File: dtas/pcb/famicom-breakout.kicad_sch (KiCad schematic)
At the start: 20 parts

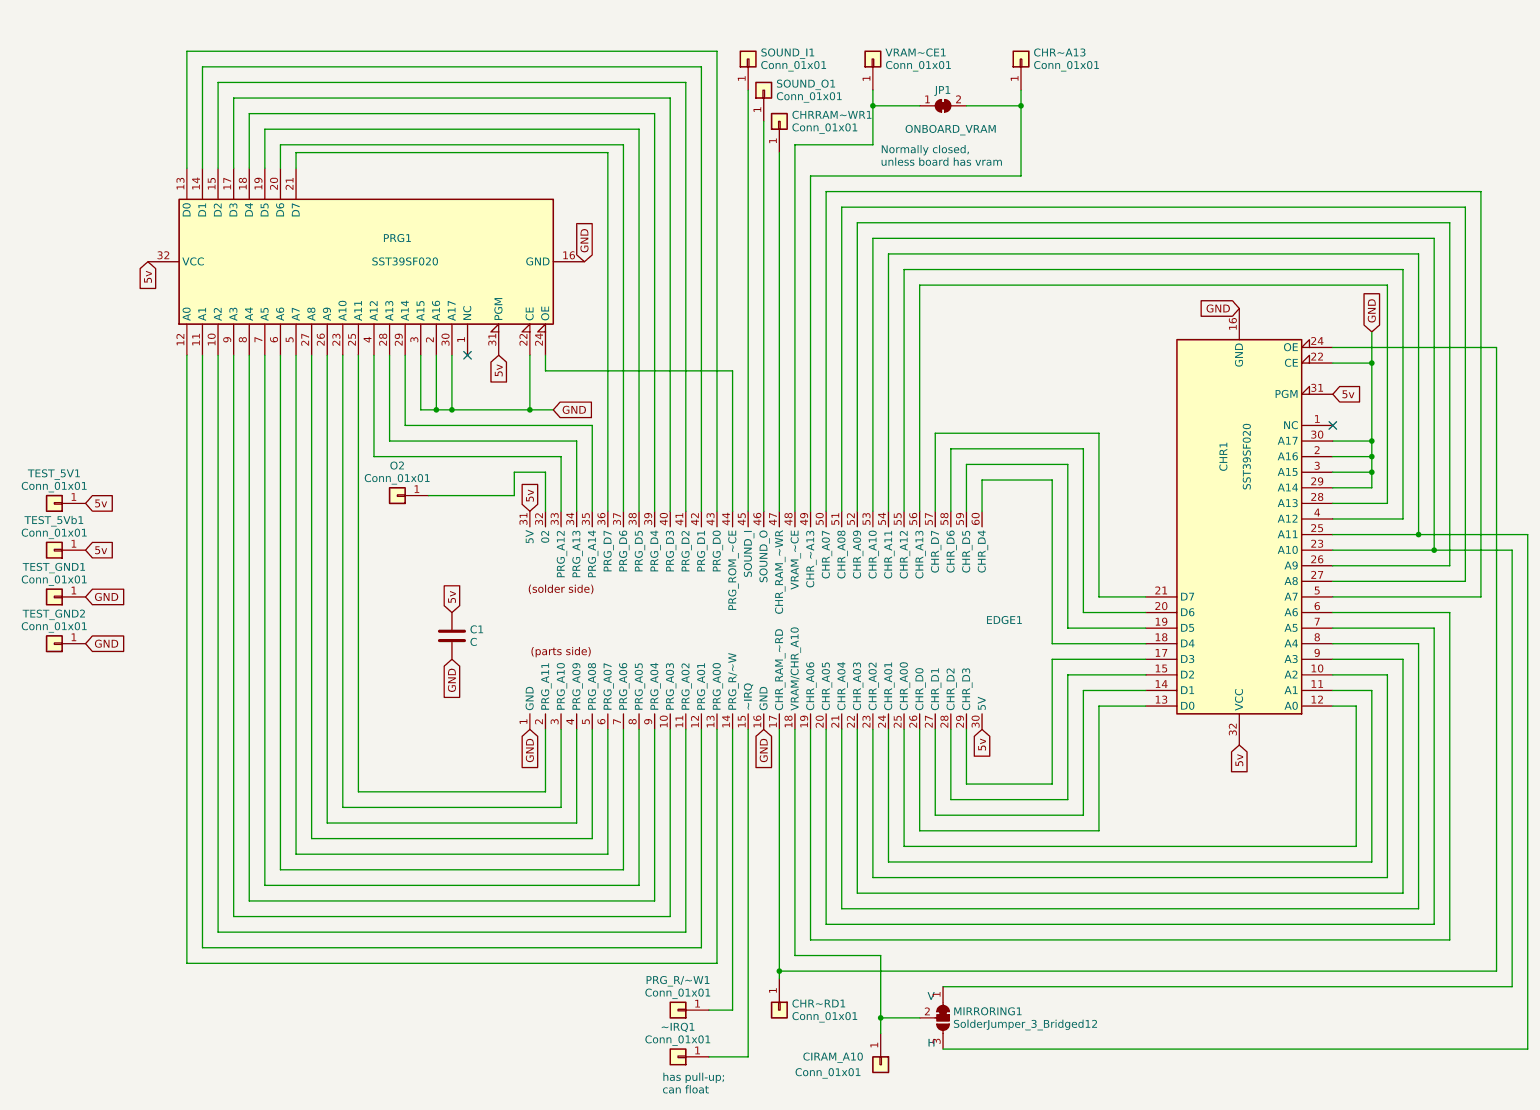
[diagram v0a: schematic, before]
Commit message: Version 2 of board, which just adds many additional test points and jumpers so I can debug the thing
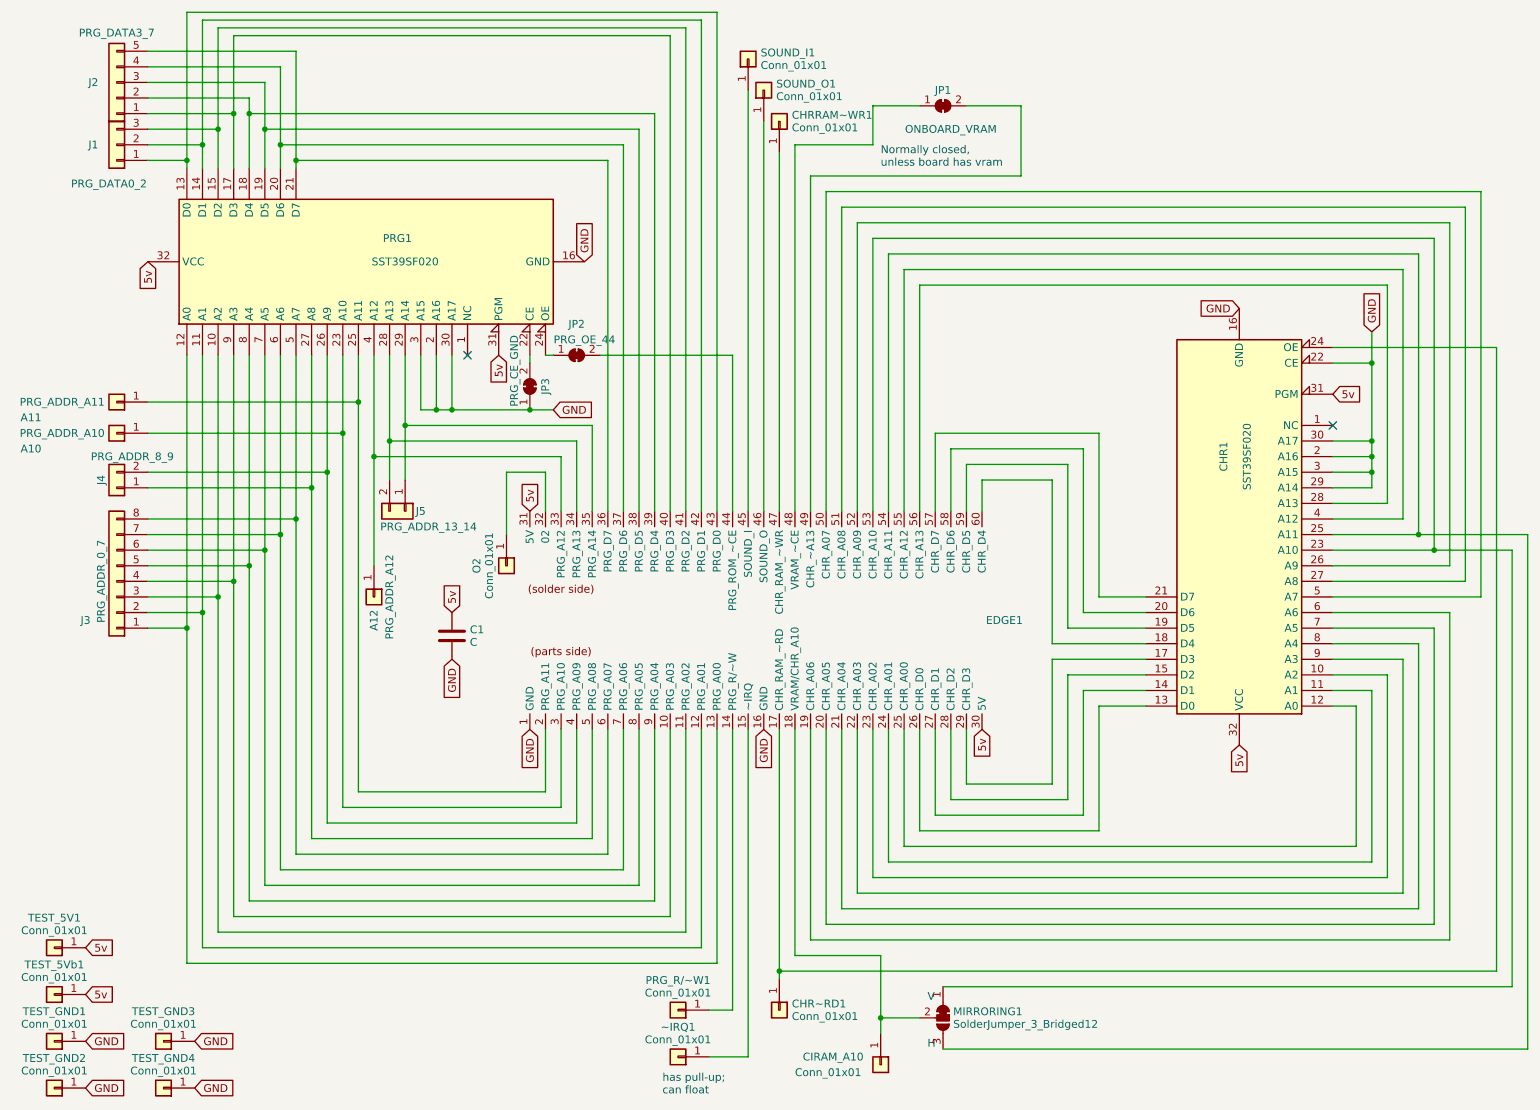
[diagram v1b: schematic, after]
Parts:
- removed CHR~A13, VRAM~CE1: Conn_01x01, Connector_PinHeader_2.54mm:PinHeader_1x01_P2.54mm_Vertical, symbol Connector_Generic:Conn_01x01
- added A10: PRG_ADDR_A10, Connector_PinHeader_2.54mm:PinHeader_1x01_P2.54mm_Vertical, symbol Connector_Generic:Conn_01x01
- added A11: PRG_ADDR_A11, Connector_PinHeader_2.54mm:PinHeader_1x01_P2.54mm_Vertical, symbol Connector_Generic:Conn_01x01
- added A12: PRG_ADDR_A12, Connector_PinHeader_2.54mm:PinHeader_1x01_P2.54mm_Vertical, symbol Connector_Generic:Conn_01x01
- added J1: PRG_DATA0_2, Connector_PinHeader_2.54mm:PinHeader_1x03_P2.54mm_Vertical, symbol Connector_Generic:Conn_01x03
- added J2: PRG_DATA3_7, Connector_PinHeader_2.54mm:PinHeader_1x05_P2.54mm_Vertical, symbol Connector_Generic:Conn_01x05
- added J3: PRG_ADDR_0_7, Connector_PinHeader_2.54mm:PinHeader_1x08_P2.54mm_Vertical, symbol Connector_Generic:Conn_01x08
- added J4: PRG_ADDR_8_9, Connector_PinHeader_2.54mm:PinHeader_1x02_P2.54mm_Vertical, symbol Connector_Generic:Conn_01x02
- added J5: PRG_ADDR_13_14, Connector_PinHeader_2.54mm:PinHeader_1x02_P2.54mm_Vertical, symbol Connector_Generic:Conn_01x02
- added JP2: PRG_OE_44, famicom:testjumperclosed, symbol Jumper:SolderJumper_2_Bridged
- added JP3: PRG_CE_GND, famicom:testjumperclosed, symbol Jumper:SolderJumper_2_Bridged
- added TEST_GND3, TEST_GND4: Conn_01x01, Connector_PinHeader_2.54mm:PinHeader_1x01_P2.54mm_Vertical, symbol Connector_Generic:Conn_01x01
- JP1: footprint Jumper:SolderJumper-2_P1.3mm_Bridged_RoundedPad1.0x1.5mm -> famicom:testjumperclosed
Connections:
- net GND: now also JP3.1 (A), TEST_GND3.1 (Pin_1), TEST_GND4.1 (Pin_1); no longer PRG1.22 (CE)
- net at EDGE1.11 (PRG_A02), PRG1.10 (A2): now also J3.3 (Pin_3)
- net at EDGE1.12 (PRG_A01), PRG1.11 (A1): now also J3.2 (Pin_2)
- net at EDGE1.13 (PRG_A00), PRG1.12 (A0): now also J3.1 (Pin_1)
- net at EDGE1.43 (PRG_D0), PRG1.13 (D0): now also J1.1 (Pin_1)
- net at EDGE1.42 (PRG_D1), PRG1.14 (D1): now also J1.2 (Pin_2)
- net at EDGE1.41 (PRG_D2), PRG1.15 (D2): now also J1.3 (Pin_3)
- net at EDGE1.40 (PRG_D3), PRG1.17 (D3): now also J2.1 (Pin_1)
- net at EDGE1.39 (PRG_D4), PRG1.18 (D4): now also J2.2 (Pin_2)
- net at EDGE1.38 (PRG_D5), PRG1.19 (D5): now also J2.3 (Pin_3)
- net at EDGE1.37 (PRG_D6), PRG1.20 (D6): now also J2.4 (Pin_4)
- net at EDGE1.36 (PRG_D7), PRG1.21 (D7): now also J2.5 (Pin_5)
- net at EDGE1.3 (PRG_A10), PRG1.23 (A10): now also A10.1 (Pin_1)
- net at PRG1.24 (OE): now also JP2.1 (A); no longer EDGE1.44 (PRG_ROM_~CE)
- net at EDGE1.2 (PRG_A11), PRG1.25 (A11): now also A11.1 (Pin_1)
- net at EDGE1.4 (PRG_A09), PRG1.26 (A9): now also J4.2 (Pin_2)
- net at EDGE1.5 (PRG_A08), PRG1.27 (A8): now also J4.1 (Pin_1)
- net at EDGE1.34 (PRG_A13), PRG1.28 (A13): now also J5.2 (Pin_2)
- net at EDGE1.35 (PRG_A14), PRG1.29 (A14): now also J5.1 (Pin_1)
- net at EDGE1.33 (PRG_A12), PRG1.4 (A12): now also A12.1 (Pin_1)
- net at EDGE1.6 (PRG_A07), PRG1.5 (A7): now also J3.8 (Pin_8)
- net at EDGE1.7 (PRG_A06), PRG1.6 (A6): now also J3.7 (Pin_7)
- net at EDGE1.8 (PRG_A05), PRG1.7 (A5): now also J3.6 (Pin_6)
- net at EDGE1.9 (PRG_A04), PRG1.8 (A4): now also J3.5 (Pin_5)
- net at EDGE1.10 (PRG_A03), PRG1.9 (A3): now also J3.4 (Pin_4)
- new net: JP3.2 (B), PRG1.22 (CE)
- new net: EDGE1.44 (PRG_ROM_~CE), JP2.2 (B)
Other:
- moved on the sheet: O2, TEST_5V1, TEST_5Vb1, TEST_GND1, TEST_GND2
